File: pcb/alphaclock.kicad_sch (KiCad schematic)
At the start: 4 parts, among them J1 Conn_01x04, J2 Conn_01x02, U1 mini_esp32, U2 L293D

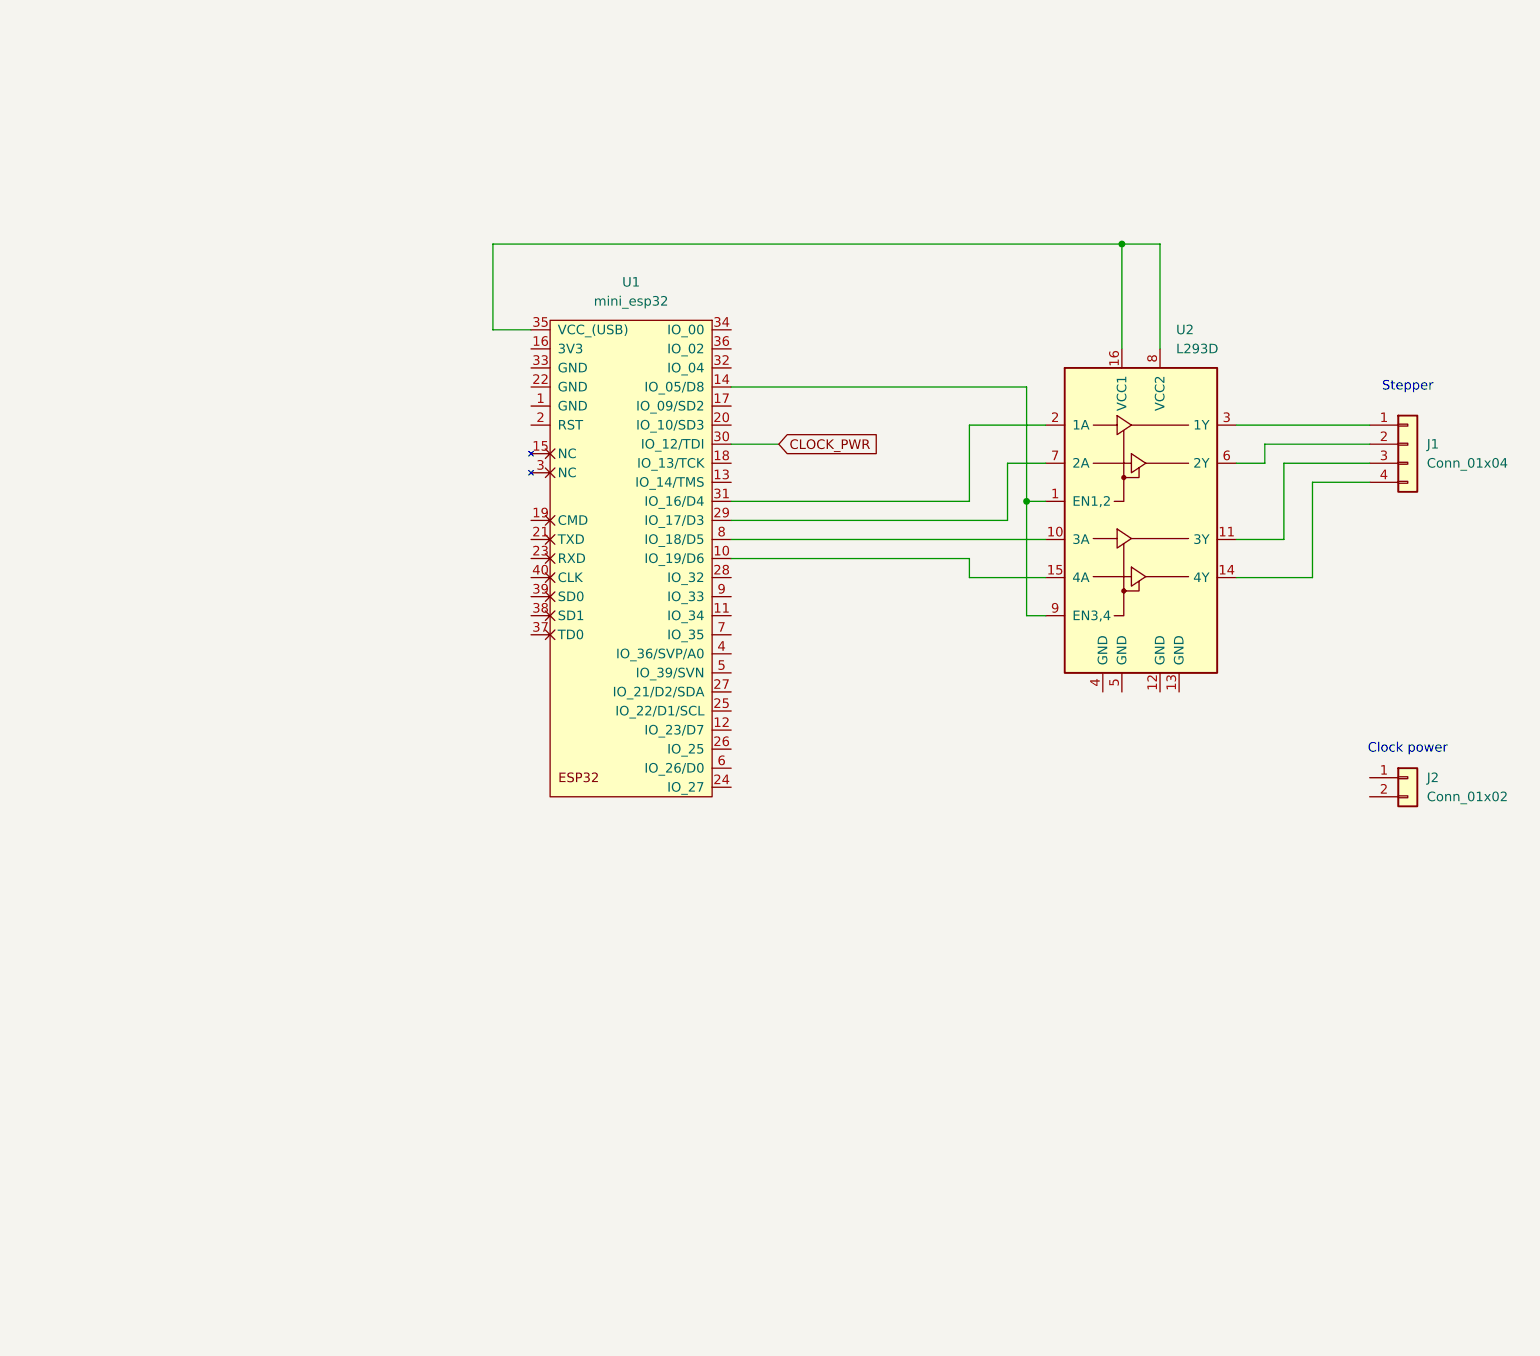
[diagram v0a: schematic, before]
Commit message: Swap IO16/17 and IO18/19 for easier layout.
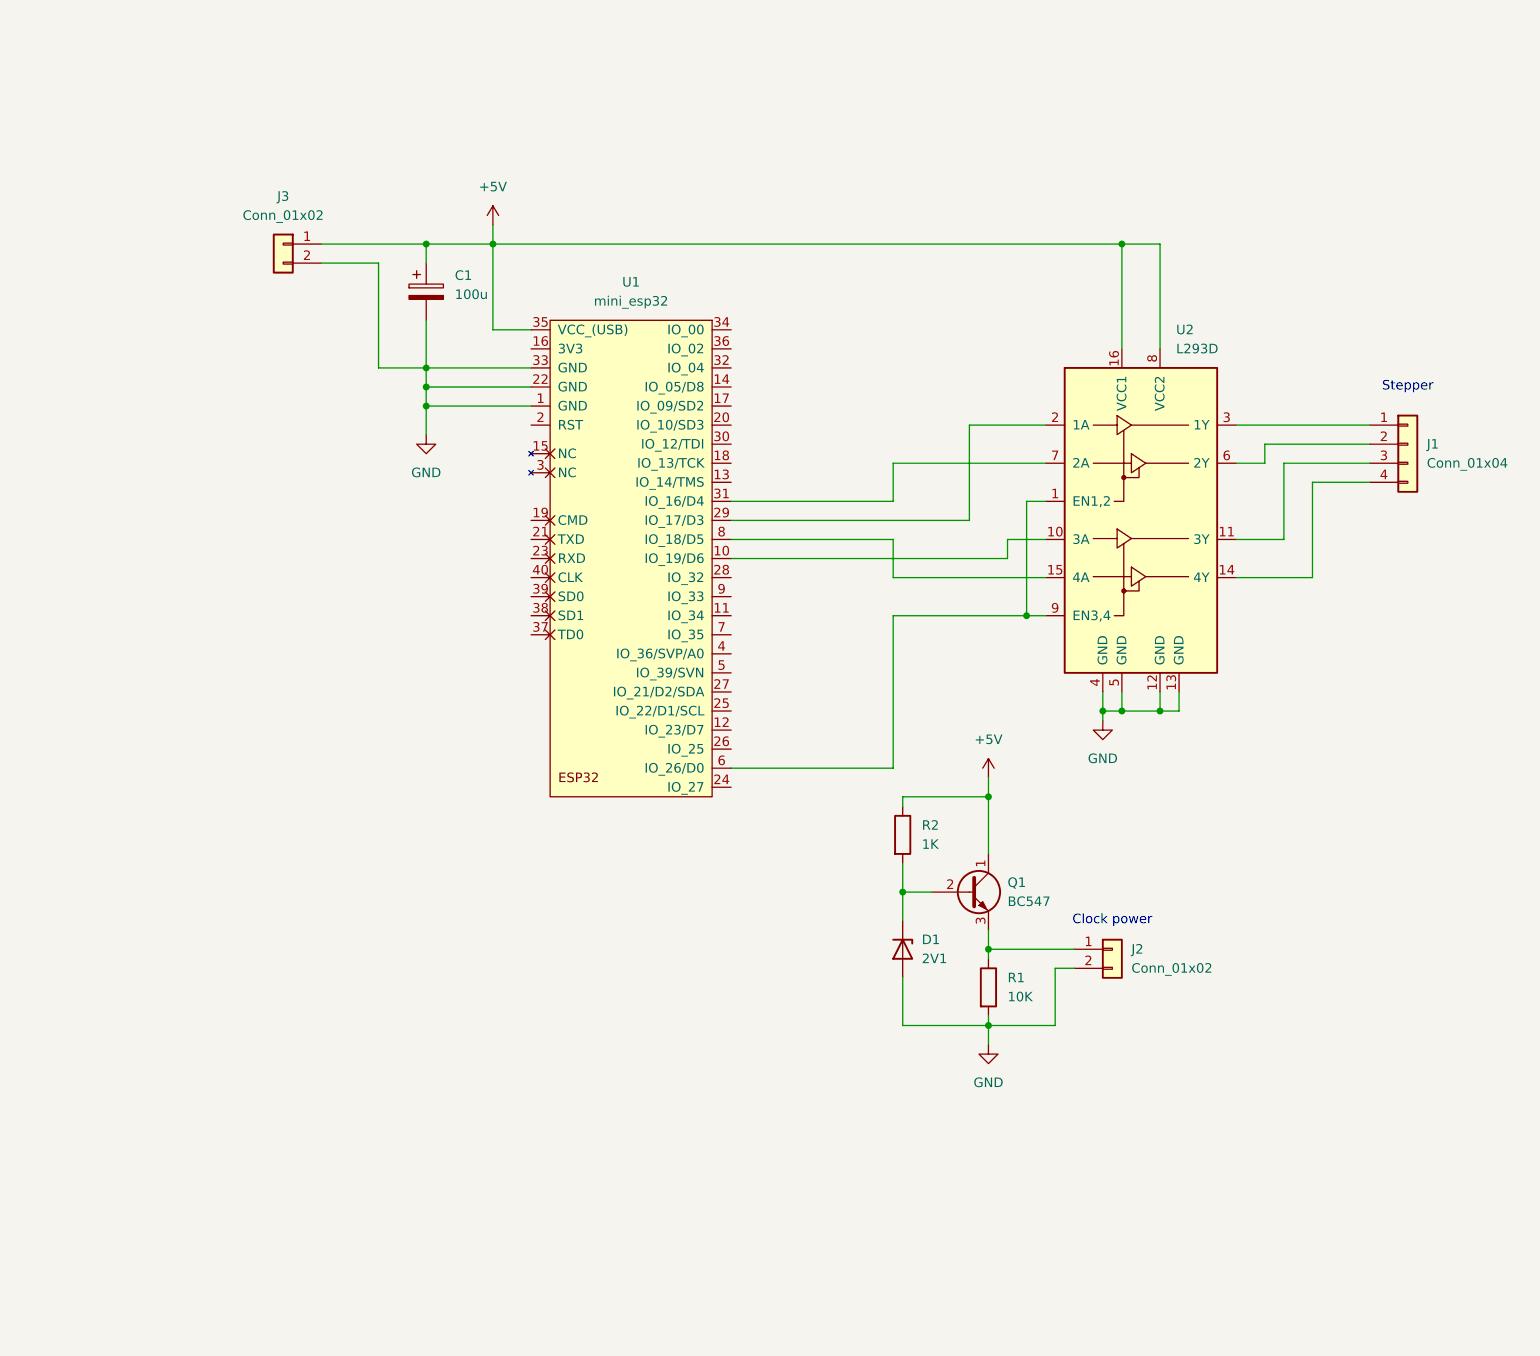
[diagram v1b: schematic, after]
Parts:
- added C1: 100u, symbol Device:C_Polarized
- added D1: 2V1, symbol Device:D_Zener
- added J3: Conn_01x02, symbol Connector_Generic:Conn_01x02
- added Q1: BC547, Package_TO_SOT_THT:TO-92_Inline, symbol Transistor_BJT:BC547
- added R1: 10K, symbol Device:R
- added R2: 1K, symbol Device:R
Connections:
- net at U2.1 (EN1,2), U2.9 (EN3,4): now also U1.6 (IO_26/D0); no longer U1.14 (IO_05/D8)
- net at U2.10 (3A): now also U1.10 (IO_19/D6); no longer U1.8 (IO_18/D5)
- net GND: now reaches U2.12 (GND)
- net GND: now also J2.2 (Pin_2), U1.1 (GND), U1.22 (GND), U1.33 (GND), U2.13 (GND), U2.4 (GND), U2.5 (GND), C1.2, D1.2 (A), J3.2 (Pin_2), R1.2
- net at U2.15 (4A): now also U1.8 (IO_18/D5); no longer U1.10 (IO_19/D6)
- net +5V: now reaches U1.35 (VCC_(USB)), U2.16 (VCC1), U2.8 (VCC2)
- net +5V: now also C1.1, J3.1 (Pin_1), Q1.1 (C), R2.1
- net at U2.2 (1A): now also U1.29 (IO_17/D3); no longer U1.31 (IO_16/D4)
- net at U2.7 (2A): now also U1.31 (IO_16/D4); no longer U1.29 (IO_17/D3)
- net at J2.1 (Pin_1): now also Q1.3 (E), R1.1
- net CLOCK_PWR: no longer names the net of U1.30 (IO_12/TDI)
- new net: D1.1 (K), Q1.2 (B), R2.2
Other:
- moved on the sheet: J2

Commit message: Remove pin numbers from ctor, update pins, add enable pin.
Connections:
- net at U2.10 (3A): now also U1.14 (IO_05/D8); no longer U1.10 (IO_19/D6)
- net at U2.15 (4A): now also U1.12 (IO_23/D7); no longer U1.8 (IO_18/D5)
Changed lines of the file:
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@@
-	(wire
-		(pts
-			(xy 114.3 88.9) (xy 151.13 88.9)
-		)
-		(stroke
-			(width 0)
-			(type default)
-		)
-	)
 	(wire
 		(pts
@@
 	(wire
 		(pts
+			(xy 121.92 91.44) (xy 156.21 91.44)
+		)
+		(stroke
+			(width 0)
+			(type default)
+		)
+	)
+	(wire
+		(pts
+			(xy 121.92 91.44) (xy 121.92 111.76)
+		)
+		(stroke
+			(width 0)
+			(type default)
+		)
+	)
+	(wire
+		(pts
 			(xy 135.89 76.2) (xy 135.89 81.28)
 		)
@@
 	(wire
 		(pts
-			(xy 151.13 88.9) (xy 151.13 86.36)
-		)
-		(stroke
-			(width 0)
-			(type default)
-		)
-	)
-	(wire
-		(pts
 			(xy 199.39 76.2) (xy 187.96 76.2)
 		)
@@
 	(wire
 		(pts
+			(xy 151.13 86.36) (xy 151.13 66.04)
+		)
+		(stroke
+			(width 0)
+			(type default)
+		)
+	)
+	(wire
+		(pts
 			(xy 135.89 81.28) (xy 114.3 81.28)
 		)
@@
 	(wire
 		(pts
+			(xy 121.92 111.76) (xy 114.3 111.76)
+		)
+		(stroke
+			(width 0)
+			(type default)
+		)
+	)
+	(wire
+		(pts
 			(xy 135.89 96.52) (xy 153.67 96.52)
 		)
@@
 	(wire
 		(pts
-			(xy 156.21 91.44) (xy 135.89 91.44)
-		)
-		(stroke
-			(width 0)
-			(type default)
-		)
-	)
-	(wire
-		(pts
 			(xy 185.42 73.66) (xy 185.42 76.2)
 		)
@@
 	(wire
 		(pts
-			(xy 135.89 86.36) (xy 114.3 86.36)
-		)
-		(stroke
-			(width 0)
-			(type default)
-		)
-	)
-	(wire
-		(pts
 			(xy 148.59 120.65) (xy 148.59 128.27)
 		)
@@
 	(wire
 		(pts
+			(xy 151.13 66.04) (xy 114.3 66.04)
+		)
+		(stroke
+			(width 0)
+			(type default)
+		)
+	)
+	(wire
+		(pts
 			(xy 171.45 46.99) (xy 171.45 60.96)
 		)
@@
 		)
 		(stroke
-			(width 0)
-			(type default)
-		)
-	)
-	(wire
-		(pts
-			(xy 135.89 91.44) (xy 135.89 86.36)
-		)
-		(stroke

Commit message: Complete routing
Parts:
- removed D1: 2V1, symbol Device:D_Zener
- removed J2: Conn_01x02, symbol Connector_Generic:Conn_01x02
- removed Q1: BC547, Package_TO_SOT_THT:TO-92_Inline, symbol Transistor_BJT:BC547
- removed R1: 10K, symbol Device:R
- removed R2: 1K, symbol Device:R
- added C2, C3, C4: 100n, Capacitor_SMD:C_0603_1608Metric, symbol Device:C
- added H1: MountingHole, MountingHole:MountingHole_3.2mm_M3, symbol Mechanical:MountingHole
- added J2, J4: Conn_01x04, Connector_JST:JST_XH_B4B-XH-A_1x04_P2.50mm_Vertical, symbol Connector_Generic:Conn_01x04
- added U3, U4: L293D, Package_DIP:DIP-16_W7.62mm, symbol Driver_Motor:L293D
- C1: footprint (none) -> Capacitor_SMD:CP_Elec_10x10
- J1: footprint (none) -> Connector_JST:JST_XH_B4B-XH-A_1x04_P2.50mm_Vertical
- J3: footprint (none) -> Connector_JST:JST_XH_B2B-XH-A_1x02_P2.50mm_Vertical
- U1: footprint (none) -> ESP32_mini:ESP32_mini
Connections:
- net +5V: now also C2.1, C3.1, C4.1, U3.16 (VCC1), U3.8 (VCC2), U4.16 (VCC1), U4.8 (VCC2)
- net GND: now also C2.2, C3.2, C4.2, U3.12 (GND), U3.13 (GND), U3.4 (GND), U3.5 (GND), U4.12 (GND), U4.13 (GND), U4.4 (GND), U4.5 (GND)
- net at U2.1 (EN1,2), U2.9 (EN3,4): now also U1.24 (IO_27); no longer U1.6 (IO_26/D0)
- net 3A: now reaches U1.14 (IO_05/D8), U2.10 (3A)
- net 3A: now also U3.10 (3A), U4.10 (3A)
- net at U1.12 (IO_23/D7): no longer U2.15 (4A)
- net at U1.29 (IO_17/D3): no longer U2.2 (1A)
- net at U1.31 (IO_16/D4): no longer U2.7 (2A)
- net 2A: now reaches U1.18 (IO_13/TCK)
- net 2A: now also U2.7 (2A), U3.7 (2A), U4.7 (2A)
- net 4A: now reaches U1.25 (IO_22/D1/SCL)
- net 4A: now also U2.15 (4A), U3.15 (4A), U4.15 (4A)
- net 1A: now reaches U1.26 (IO_25)
- net 1A: now also U2.2 (1A), U3.2 (1A), U4.2 (1A)
- net EN2: now reaches U1.28 (IO_32)
- net EN2: now also U3.1 (EN1,2), U3.9 (EN3,4)
- net EN3: now reaches U1.30 (IO_12/TDI)
- net EN3: now also U4.1 (EN1,2), U4.9 (EN3,4)
- new net: J4.3 (Pin_3), U4.11 (3Y)
- new net: J4.4 (Pin_4), U4.14 (4Y)
- new net: J4.1 (Pin_1), U4.3 (1Y)
- new net: J4.2 (Pin_2), U4.6 (2Y)
- new net: J2.3 (Pin_3), U3.11 (3Y)
- new net: J2.4 (Pin_4), U3.14 (4Y)
- new net: J2.1 (Pin_1), U3.3 (1Y)
- new net: J2.2 (Pin_2), U3.6 (2Y)
- no-connect marks 0 -> 27
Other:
- note removed: "Clock power"
- moved on the sheet: C1, J1, J3, U1, U2
